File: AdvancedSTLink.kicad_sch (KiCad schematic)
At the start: 56 parts, among them J1 Conn_01x03, J2 Conn_01x02_Pin, J3 Conn_01x06, J4 USB_C_Receptacle_USB2.0, J5 Conn_01x05, Q1 S8050, SW2 SW_Push, U1 STM32F205RETx, U2 XC6206P332MR, U3 USBLC6-2SC6, U4 SPX1117-3.3, U5 USBLC6-2SC6, U6 USBLC6-2SC6, U7 USBLC6-2SC6, Y1 X322512MSB4SI

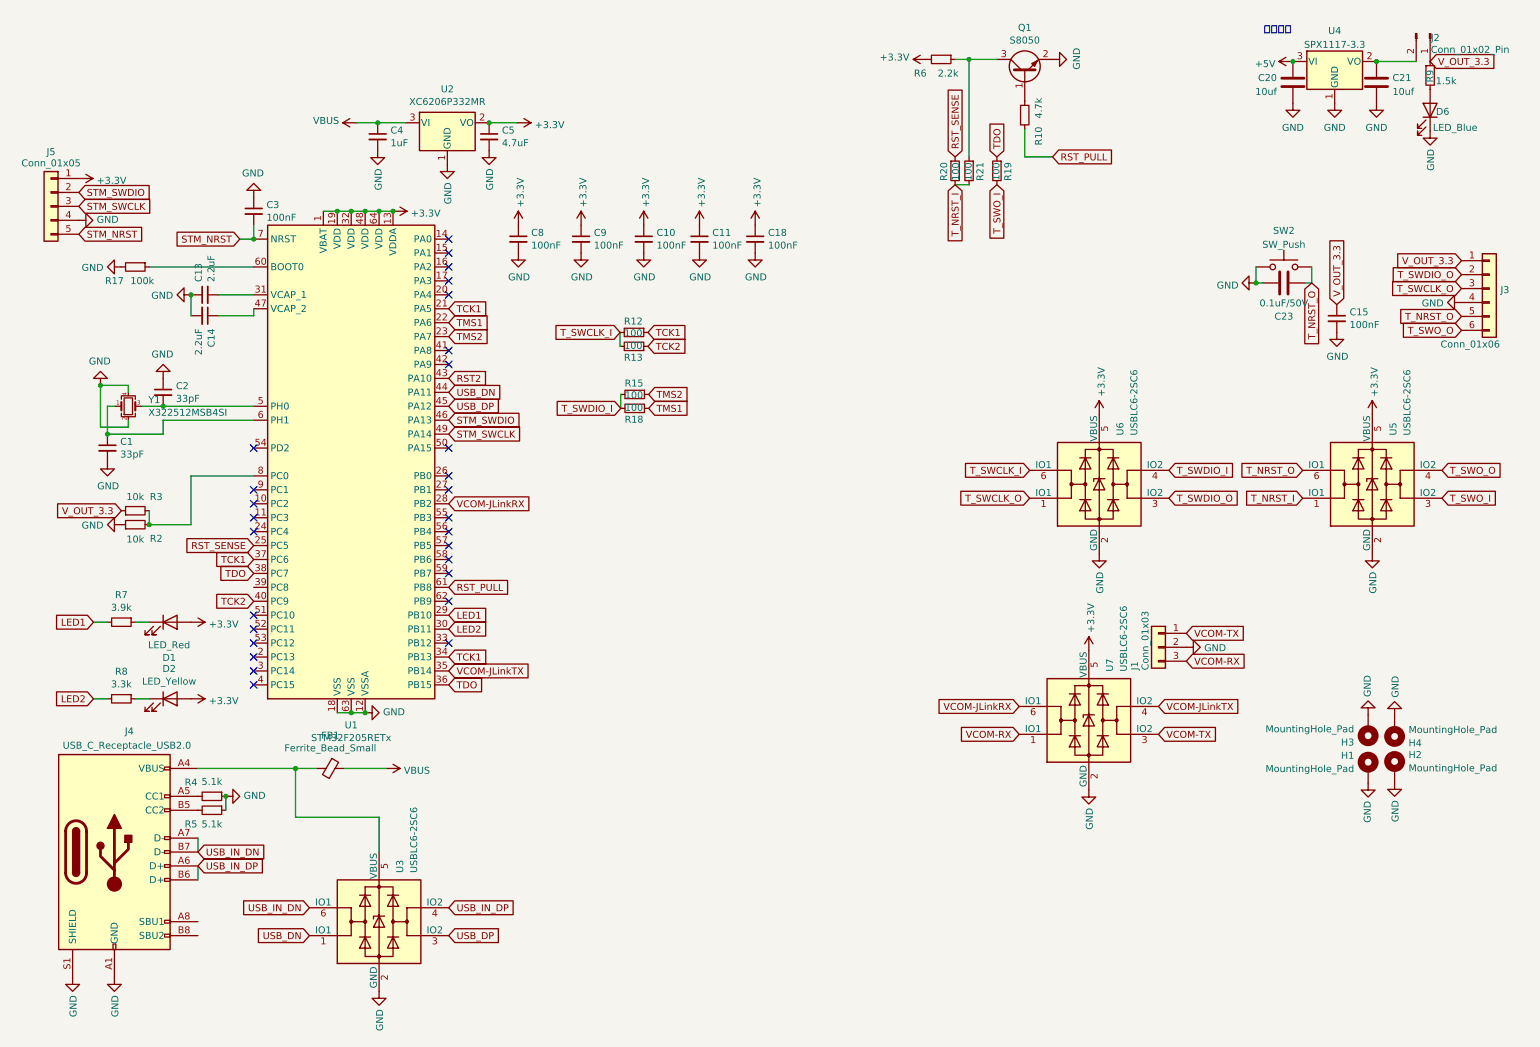
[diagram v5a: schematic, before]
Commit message: 改正电源, 改正电阻值, 改正上拉
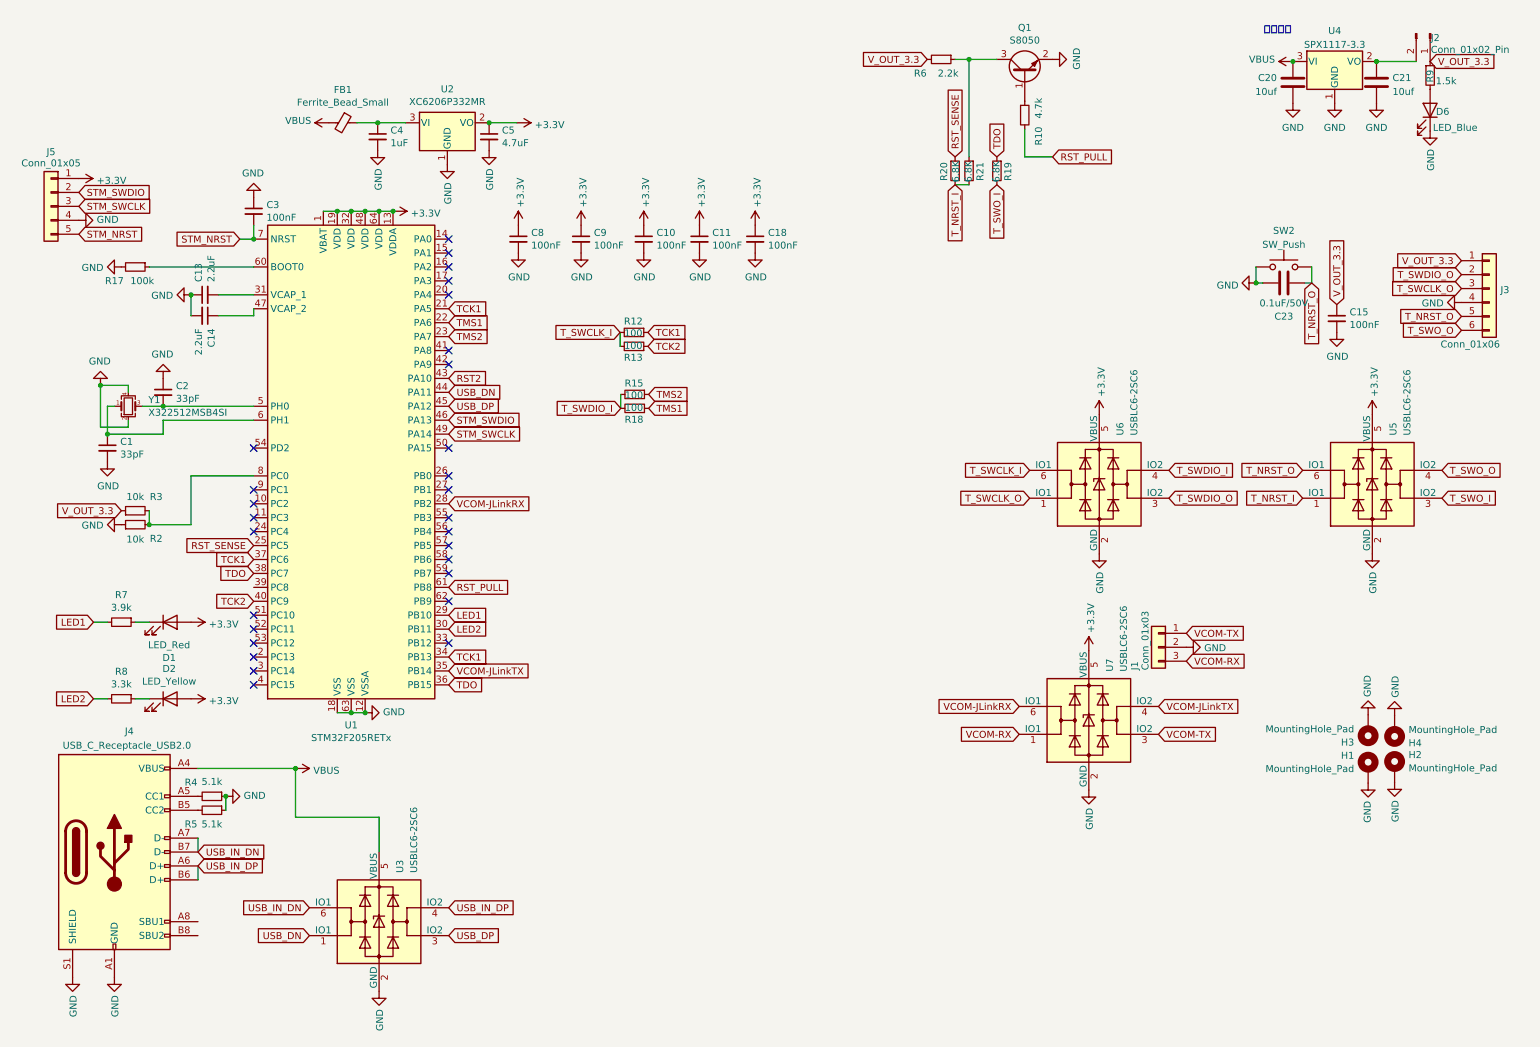
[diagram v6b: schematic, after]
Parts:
- J5: footprint KisonNew:JLinkDebugSWD -> KisonNew:JLinkSWDNonThroughHole
- R19, R20, R21: value 100 -> 6.8K
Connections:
- net +5V is gone; now on net VBUS: C20.1, U4.3 (VI)
- net +3V3: no longer R6.2
- net VBUS: now also FB1.2, J4.A4 (VBUS), J4.A9 (VBUS), J4.B4 (VBUS), J4.B9 (VBUS), U3.5 (VBUS); no longer C4.1, FB1.1, U2.3 (VI)
- net V_OUT_3.3: now also R6.2
- new net: C4.1, FB1.1, U2.3 (VI)
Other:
- moved on the sheet: FB1
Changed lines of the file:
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@@
   (junction (at 54.102 52.324) (diameter 0) (color 0 0 0 0)
   )
+  (junction (at 61.722 148.844) (diameter 0) (color 0 0 0 0)
+  )
   (junction (at 76.962 47.244) (diameter 0) (color 0 0 0 0)
   )
@@
   (junction (at 79.502 47.244) (diameter 0) (color 0 0 0 0)
   )
-  (junction (at 61.722 148.844) (diameter 0) (color 0 0 0 0)
-  )
   (junction (at 27.432 87.884) (diameter 0) (color 0 0 0 0)
   )
@@
     (stroke (width 0) (type default))
   )
-  (wire (pts (xy 61.722 148.844) (xy 65.532 148.844))
-    (stroke (width 0) (type default))
-  )
   (wire (pts (xy 71.882 138.684) (xy 74.422 138.684))
     (stroke (width 0) (type default))
@@
     (stroke (width 0) (type default))
   )
-  (wire (pts (xy 70.612 148.844) (xy 78.232 148.844))
-    (stroke (width 0) (type default))
-  )
   (wire (pts (xy 69.342 138.684) (xy 71.882 138.684))
     (stroke (width 0) (type default))
@@
     )
   )
+  (global_label "V_OUT_3.3" (shape input) (at 176.911 19.558 180)
+    (effects (font (size 1.27 1.27)) (justify right))
+    (property "Intersheetrefs" "${INTERSHEET_REFS}" (at 176.911 19.558 0)
+      (effects (font (size 1.27 1.27)) hide)
+    )
+  )
   (global_label "TMS2" (shape input) (at 126.111 80.645 0)
     (effects (font (size 1.27 1.27)) (justify left))
@@
     )
   )
-  (symbol (lib_id "power:VBUS") (at 78.232 148.844 270) (unit 1)
+  (symbol (lib_id "power:VBUS") (at 61.722 148.844 270) (unit 1)
     (in_bom yes) (on_board yes) (dnp no)
-    (property "Reference" "#PWR09" (at 74.422 148.844 0)
+    (property "Reference" "#PWR09" (at 57.912 148.844 0)
       (effects (font (size 1.27 1.27)) hide)
     )
-    (property "Value" "VBUS" (at 81.4832 149.225 90)
+    (property "Value" "VBUS" (at 64.9732 149.225 90)
       (effects (font (size 1.27 1.27)) (justify left))
     )
-    (property "Footprint" "" (at 78.232 148.844 0)
+    (property "Footprint" "" (at 61.722 148.844 0)
       (effects (font (size 1.27 1.27)) hide)
     )
-    (property "Datasheet" "" (at 78.232 148.844 0)
+    (property "Datasheet" "" (at 61.722 148.844 0)
       (effects (font (size 1.27 1.27)) hide)
     )
@@
     )
   )
-  (symbol (lib_id "power:VBUS") (at 72.898 31.115 90) (unit 1)
+  (symbol (lib_id "power:VBUS") (at 67.818 31.115 90) (unit 1)
     (in_bom yes) (on_board yes) (dnp no)
-    (property "Reference" "#PWR010" (at 76.708 31.115 0)
+    (property "Reference" "#PWR010" (at 71.628 31.115 0)
       (effects (font (size 1.27 1.27)) hide)
     )
-    (property "Value" "VBUS" (at 69.6722 30.734 90)
+    (property "Value" "VBUS" (at 64.5922 30.734 90)
       (effects (font (size 1.27 1.27)) (justify left))
     )
-    (property "Footprint" "" (at 72.898 31.115 0)
+    (property "Footprint" "" (at 67.818 31.115 0)
       (effects (font (size 1.27 1.27)) hide)
     )
-    (property "Datasheet" "" (at 72.898 31.115 0)
+    (property "Datasheet" "" (at 67.818 31.115 0)
       (effects (font (size 1.27 1.27)) hide)
     )
@@
     )
   )
-  (symbol (lib_id "AdvancedSTLink-rescue:Ferrite_Bead_Small-Device") (at 68.072 148.844 270) (unit 1)
+  (symbol (lib_id "AdvancedSTLink-rescue:Ferrite_Bead_Small-Device") (at 70.358 31.115 270) (unit 1)
     (in_bom yes) (on_board yes) (dnp no)
-    (property "Reference" "FB1" (at 68.072 142.8242 90)
+    (property "Reference" "FB1" (at 70.358 25.0952 90)
       (effects (font (size 1.27 1.27)))
     )
-    (property "Value" "Ferrite_Bead_Small" (at 68.072 145.1356 90)
+    (property "Value" "Ferrite_Bead_Small" (at 70.358 27.4066 90)
       (effects (font (size 1.27 1.27)))
     )
-    (property "Footprint" "Inductor_SMD:L_0805_2012Metric" (at 68.072 147.066 90)
+    (property "Footprint" "Inductor_SMD:L_0805_2012Metric" (at 70.358 29.337 90)
       (effects (font (size 1.27 1.27)) hide)
     )
-    (property "Datasheet" "~" (at 68.072 148.844 0)
+    (property "Datasheet" "~" (at 70.358 31.115 0)
       (effects (font (size 1.27 1.27)) hide)
     )
@@
     )
   )
-  (symbol (lib_id "AdvancedSTLink-rescue:+3.3V-power") (at 176.911 19.558 90) (unit 1)
-    (in_bom yes) (on_board yes) (dnp no)
-    (property "Reference" "#PWR0112" (at 180.721 19.558 0)
-      (effects (font (size 1.27 1.27)) hide)
-    )
-    (property "Value" "+3.3V" (at 173.6598 19.177 90)
-      (effects (font (size 1.27 1.27)) (justify left))
-    )
-    (property "Footprint" "" (at 176.911 19.558 0)
-      (effects (font (size 1.27 1.27)) hide)
-    )
-    (property "Datasheet" "" (at 176.911 19.558 0)
-      (effects (font (size 1.27 1.27)) hide)
-    )
-    (pin "1")
-    (instances
-      (project "AdvancedSTLink"
-        (path "/08ba500b-6f18-4ea2-9e8c-39dcb944023d"
-          (reference "#PWR0112") (unit 1)
-        )
-      )
-    )
-  )
   (symbol (lib_id "power:GND") (at 199.771 19.558 90) (unit 1)
     (in_bom yes) (on_board yes) (dnp no)
@@
       (effects (font (size 1.27 1.27)))
     )
-    (property "Value" "100" (at 184.404 40.005 90)
+    (property "Value" "6.8K" (at 184.404 40.005 90)
       (effects (font (size 1.27 1.27)))
     )
@@
     )
   )
-  (symbol (lib_id "power:+5V") (at 243.586 19.939 90) (unit 1)
-    (in_bom yes) (on_board yes) (dnp no) (fields_autoplaced)
-    (property "Reference" "#PWR018" (at 247.396 19.939 0)
-      (effects (font (size 1.27 1.27)) hide)
-    )
-    (property "Value" "+5V" (at 240.4111 20.3728 90)
-      (effects (font (size 1.27 1.27)) (justify left))
-    )
-    (property "Footprint" "" (at 243.586 19.939 0)
-      (effects (font (size 1.27 1.27)) hide)
-    )
-    (property "Datasheet" "" (at 243.586 19.939 0)
-      (effects (font (size 1.27 1.27)) hide)
-    )
-    (pin "1")
-    (instances
-      (project "AdvancedSTLink"
-        (path "/08ba500b-6f18-4ea2-9e8c-39dcb944023d"
-          (reference "#PWR018") (unit 1)
-        )
-      )
-      (project "main-control"
-        (path "/82893348-90fa-45f5-80a2-57562324326c"
-          (reference "#PWR0148") (unit 1)
-        )
-      )
-    )
-  )
   (symbol (lib_id "power:GND") (at 224.155 126.746 90) (mirror x) (unit 1)
     (in_bom yes) (on_board yes) (dnp no)
@@
       (effects (font (size 1.27 1.27)))
     )
-    (property "Footprint" "KisonNew:JLinkDebugSWD" (at 17.145 46.355 0)
+    (property "Footprint" "KisonNew:JLinkSWDNonThroughHole" (at 17.145 46.355 0)
       (effects (font (size 1.27 1.27)) hide)
     )
@@
     )
   )
+  (symbol (lib_id "power:VBUS") (at 243.586 19.939 90) (unit 1)
+    (in_bom yes) (on_board yes) (dnp no)
+    (property "Reference" "#PWR029" (at 247.396 19.939 0)
+      (effects (font (size 1.27 1.27)) hide)
+    )
+    (property "Value" "VBUS" (at 240.3348 19.558 90)
+      (effects (font (size 1.27 1.27)) (justify left))
+    )
+    (property "Footprint" "" (at 243.586 19.939 0)
+      (effects (font (size 1.27 1.27)) hide)
+    )
+    (property "Datasheet" "" (at 243.586 19.939 0)
+      (effects (font (size 1.27 1.27)) hide)
+    )
+    (pin "1")
+    (instances
+      (project "AdvancedSTLink"
+        (path "/08ba500b-6f18-4ea2-9e8c-39dcb944023d"
+          (reference "#PWR029") (unit 1)
+        )
+      )
+    )
+  )
   (symbol (lib_id "Device:R_Small") (at 181.991 39.878 0) (unit 1)
     (in_bom yes) (on_board yes) (dnp no)
@@
       (effects (font (size 1.27 1.27)))
     )
-    (property "Value" "100" (at 182.118 40.005 90)
+    (property "Value" "6.8K" (at 182.118 40.005 90)
       (effects (font (size 1.27 1.27)))
     )
@@
       (effects (font (size 1.27 1.27)))
     )
-    (property "Value" "100" (at 189.484 40.005 90)
+    (property "Value" "6.8K" (at 189.484 40.005 90)
       (effects (font (size 1.27 1.27)))
     )

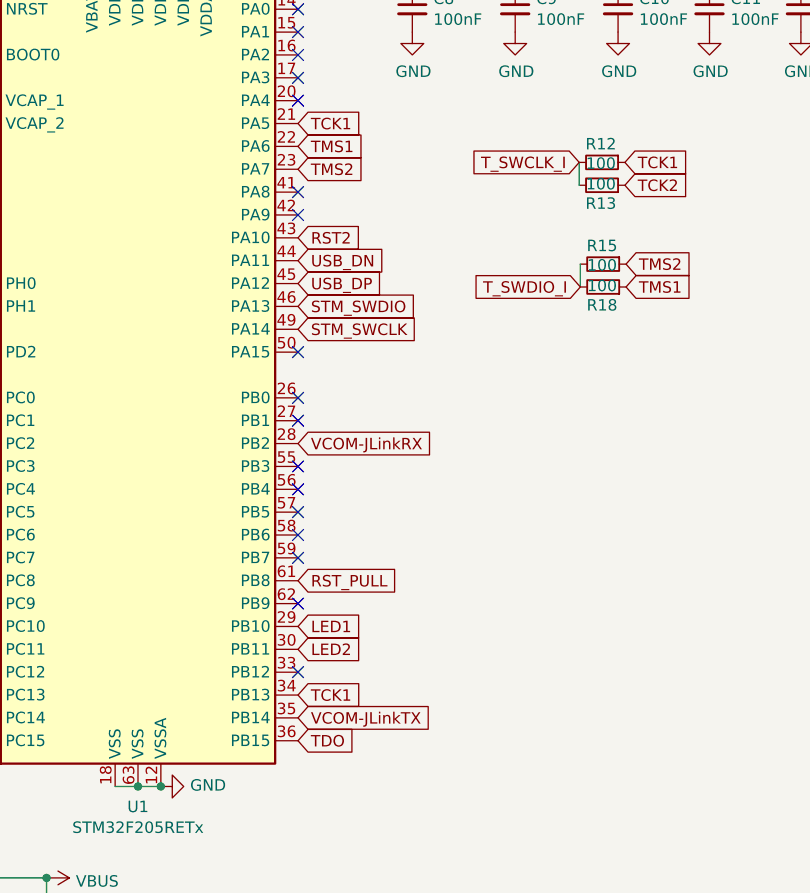
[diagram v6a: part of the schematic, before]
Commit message: 更新原理图以及layout
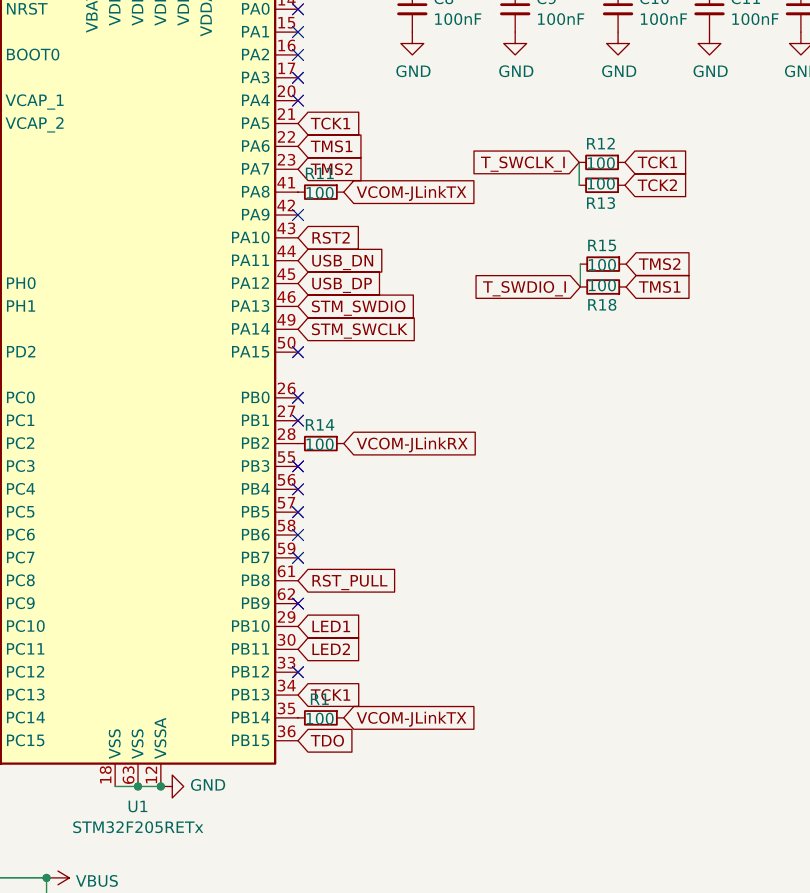
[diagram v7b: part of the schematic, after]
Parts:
- added R1, R11, R14: 100, Resistor_SMD:R_0402_1005Metric, symbol Device:R_Small
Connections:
- net VCOM-JLinkRX: now also R14.1; no longer U1.28 (PB2)
- net VCOM-JLinkTX: now also R1.1, R11.1; no longer U1.35 (PB14)
- net at U1.41 (PA8): now also R11.2
- new net: R14.2, U1.28 (PB2)
- new net: R1.2, U1.35 (PB14)
- no-connect marks 28 -> 27
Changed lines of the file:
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@@
   (no_connect (at 89.662 103.124))
   (no_connect (at 89.662 52.324))
-  (no_connect (at 89.662 72.644))
   (no_connect (at 89.662 98.044))
   (no_connect (at 89.662 113.284))
@@
     )
   )
+  (global_label "VCOM-JLinkTX" (shape input) (at 94.742 72.644 0) (fields_autoplaced)
+    (effects (font (size 1.27 1.27)) (justify left))
+    (property "Intersheetrefs" "${INTERSHEET_REFS}" (at 110.6612 72.644 0)
+      (effects (font (size 1.27 1.27)) (justify left) hide)
+    )
+  )
   (global_label "TMS2" (shape input) (at 89.662 70.104 0)
     (effects (font (size 1.27 1.27)) (justify left))
@@
     )
   )
-  (global_label "VCOM-JLinkTX" (shape input) (at 89.662 131.064 0) (fields_autoplaced)
+  (global_label "VCOM-JLinkTX" (shape input) (at 94.742 131.064 0) (fields_autoplaced)
     (effects (font (size 1.27 1.27)) (justify left))
-    (property "Intersheetrefs" "${INTERSHEET_REFS}" (at 105.5812 131.064 0)
+    (property "Intersheetrefs" "${INTERSHEET_REFS}" (at 110.6612 131.064 0)
       (effects (font (size 1.27 1.27)) (justify left) hide)
     )
@@
     )
   )
-  (global_label "VCOM-JLinkRX" (shape input) (at 89.662 100.584 0) (fields_autoplaced)
+  (global_label "VCOM-JLinkRX" (shape input) (at 94.742 100.584 0) (fields_autoplaced)
     (effects (font (size 1.27 1.27)) (justify left))
-    (property "Intersheetrefs" "${INTERSHEET_REFS}" (at 105.8836 100.584 0)
+    (property "Intersheetrefs" "${INTERSHEET_REFS}" (at 110.9636 100.584 0)
       (effects (font (size 1.27 1.27)) (justify left) hide)
     )
@@
     )
   )
+  (symbol (lib_id "Device:R_Small") (at 92.202 72.644 270) (unit 1)
+    (in_bom yes) (on_board yes) (dnp no)
+    (property "Reference" "R11" (at 92.075 70.612 90)
+      (effects (font (size 1.27 1.27)))
+    )
+    (property "Value" "100" (at 92.075 72.771 90)
+      (effects (font (size 1.27 1.27)))
+    )
+    (property "Footprint" "Resistor_SMD:R_0402_1005Metric" (at 92.202 72.644 0)
+      (effects (font (size 1.27 1.27)) hide)
+    )
+    (property "Datasheet" "~" (at 92.202 72.644 0)
+      (effects (font (size 1.27 1.27)) hide)
+    )
+    (pin "1")
+    (pin "2")
+    (instances
+      (project "AdvancedSTLink"
+        (path "/08ba500b-6f18-4ea2-9e8c-39dcb944023d"
+          (reference "R11") (unit 1)
+        )
+      )
+    )
+  )
   (symbol (lib_id "Connector_Generic:Conn_01x05") (at 17.145 46.355 0) (mirror y) (unit 1)
     (in_bom yes) (on_board yes) (dnp no) (fields_autoplaced)
@@
     )
   )
+  (symbol (lib_id "Device:R_Small") (at 92.202 100.584 270) (unit 1)
+    (in_bom yes) (on_board yes) (dnp no)
+    (property "Reference" "R14" (at 92.075 98.552 90)
+      (effects (font (size 1.27 1.27)))
+    )
+    (property "Value" "100" (at 92.075 100.711 90)
+      (effects (font (size 1.27 1.27)))
+    )
+    (property "Footprint" "Resistor_SMD:R_0402_1005Metric" (at 92.202 100.584 0)
+      (effects (font (size 1.27 1.27)) hide)
+    )
+    (property "Datasheet" "~" (at 92.202 100.584 0)
+      (effects (font (size 1.27 1.27)) hide)
+    )
+    (pin "1")
+    (pin "2")
+    (instances
+      (project "AdvancedSTLink"
+        (path "/08ba500b-6f18-4ea2-9e8c-39dcb944023d"
+          (reference "R14") (unit 1)
+        )
+      )
+    )
+  )
   (symbol (lib_id "Connector_Generic:Conn_01x03") (at 219.075 126.746 0) (mirror y) (unit 1)
     (in_bom yes) (on_board yes) (dnp no)
@@
         )
       )
+    )
+  )
+  (symbol (lib_id "Device:R_Small") (at 92.202 131.064 270) (unit 1)
+    (in_bom yes) (on_board yes) (dnp no)
+    (property "Reference" "R1" (at 92.075 129.032 90)
+      (effects (font (size 1.27 1.27)))
+    )
+    (property "Value" "100" (at 92.075 131.191 90)
+      (effects (font (size 1.27 1.27)))
+    )
+    (property "Footprint" "Resistor_SMD:R_0402_1005Metric" (at 92.202 131.064 0)
+      (effects (font (size 1.27 1.27)) hide)
+    )
+    (property "Datasheet" "~" (at 92.202 131.064 0)
+      (effects (font (size 1.27 1.27)) hide)
+    )
+    (pin "1")
+    (pin "2")
+    (instances
+      (project "AdvancedSTLink"
+        (path "/08ba500b-6f18-4ea2-9e8c-39dcb944023d"
+          (reference "R1") (unit 1)
+        )
+      )
